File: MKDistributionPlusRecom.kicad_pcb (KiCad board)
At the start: 2 copper layers, 22.5 x 17 mm, 5 parts, among them U1 LM7805CT

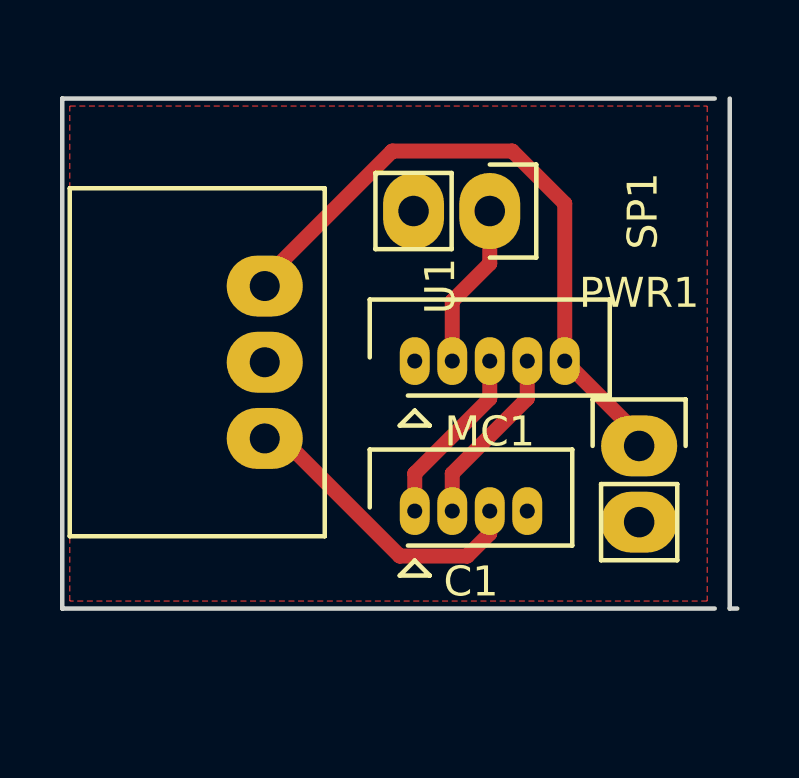
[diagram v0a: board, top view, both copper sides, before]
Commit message: Added a second 5-pin Molex connector for BLCtrl
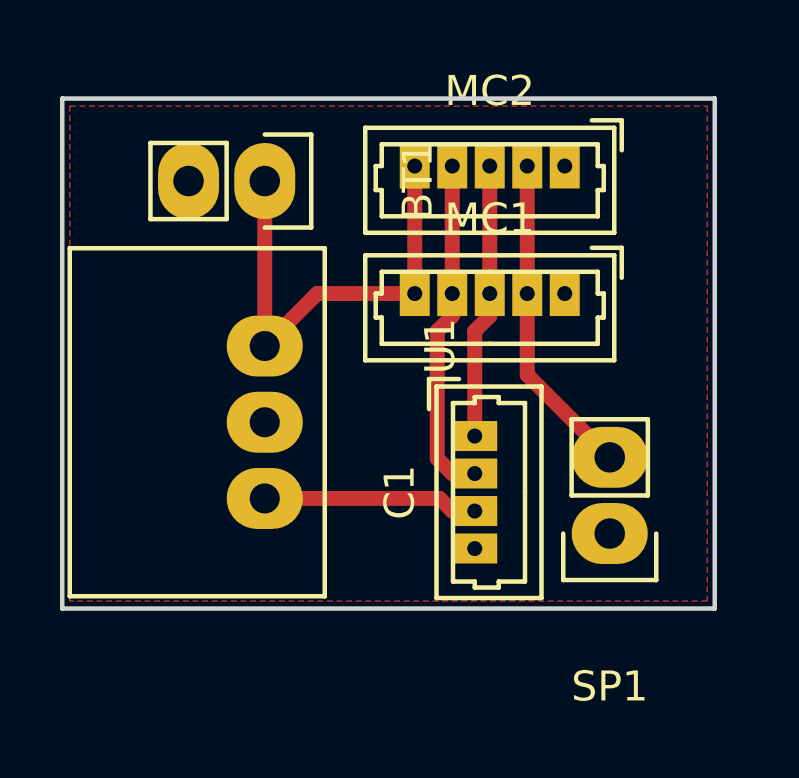
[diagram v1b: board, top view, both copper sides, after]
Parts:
- removed PWR1: POWER, Pin_Headers:Pin_Header_Straight_1x02
- added BT1: Battery, Pin_Headers:Pin_Header_Straight_1x02, F.Cu at (145.0, 91.5)
- added MC2: MotorCtrl, Connectors_Molex:Molex_PicoBlade_53047-0510_05x1.25mm_Straight, F.Cu at (155.0, 91.0)
- C1: footprint Connectors_Molex:Molex_PicoBlade_53047-0410 -> Connectors_Molex:Molex_PicoBlade_53047-0410_04x1.25mm_Straight
- MC1: footprint Connectors_Molex:Molex_PicoBlade_53047-0510 -> Connectors_Molex:Molex_PicoBlade_53047-0510_05x1.25mm_Straight
- moved SP1 11.5 mm to (156.5, 103.2), turned to 180 degrees
- moved MC1 5.48 mm to (155.0, 95.2), turned to 180 degrees
- moved C1 3.20 mm to (152.0, 100.0), turned to 270 degrees
- moved U1 2.00 mm to (145.0, 97.0)
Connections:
- SP1 pad 1: Net-(MC1-Pad2) -> GND
- SP1 pad 2: GND -> Net-(MC1-Pad2)
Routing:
- net +BATT: track 21.8 -> 15.8 mm
- net Net-(C1-Pad2): track 6.04 -> 11.4 mm
- net Net-(MC1-Pad2): track 5.52 -> 10.8 mm
- net Net-(C1-Pad1): track 6.04 -> 9.21 mm
- net Net-(C1-Pad3): track 10.2 -> 7.17 mm
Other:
- board size 22.5 x 17 mm -> 21.8 x 17 mm
